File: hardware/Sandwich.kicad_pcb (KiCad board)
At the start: 2 copper layers, 80 x 100.2 mm, 20 parts, among them P1 CONN_01X20, P2 CONN_01X06, P3 VGA_OUT, Q1 PZT2222A, U1 P8X32A-D40, U2 24C512, Y1 5MHz

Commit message: Updated schematics, PCB layout is nearly done.
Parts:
- D1: footprint LEDs:LED-3MM -> LEDs:LED-5MM
- moved Q1 118.8 mm to (187.0, 109.8)
- moved U2 118.5 mm to (209.2, 111.9)
- moved P2 118.1 mm to (180.3, 91.2)
- moved U1 117.7 mm to (178.8, 96.0)
- moved Y1 116.3 mm to (200.0, 108.2)
- moved P1 100.6 mm to (152.0, 144.2)
- moved R7 100.4 mm to (211.4, 144.2)
- moved R11 100.3 mm to (211.4, 140.9)
- moved R6 100.3 mm to (211.4, 137.6)
- moved R10 100.3 mm to (211.4, 134.2)
- moved R5 100.2 mm to (211.4, 130.9)
- moved R9 100.2 mm to (211.4, 127.5)
- moved R4 100.2 mm to (211.4, 124.2)
- moved R8 100.2 mm to (211.4, 120.8)
- moved R1 100.1 mm to (211.4, 117.5)
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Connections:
- P2 pad 5: PROP_DTR -> GND
- P2 pad 6: GND -> PROP_DTR
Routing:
- net 5V: track 0.00 -> 142.7 mm
- net 3.3V: track 45.8 -> 110.0 mm
- net Net-(P1-Pad20): track 0.00 -> 58.1 mm
- net Net-(U1-Pad37): track 0.00 -> 36.0 mm
- net Net-(P1-Pad9): track 0.00 -> 31.0 mm
- net Net-(P1-Pad16): track 0.00 -> 31.0 mm
- net Net-(P1-Pad14): track 0.00 -> 31.0 mm
- net Net-(P1-Pad15): track 0.00 -> 31.0 mm
- net Net-(P1-Pad13): track 0.00 -> 31.0 mm
- net Net-(P1-Pad12): track 0.00 -> 31.0 mm
- net Net-(P1-Pad11): track 0.00 -> 31.0 mm
- net Net-(P1-Pad10): track 0.00 -> 31.0 mm
- net PROP_RX: track 28.2 -> 0.00 mm
- net Net-(R3-Pad1): track 0.00 -> 27.4 mm
- net Net-(C1-Pad1): track 41.8 -> 22.0 mm
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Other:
- board size 80 x 100.2 mm -> 80 x 65 mm

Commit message: Production ready VGA board.
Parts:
- moved C1 49.9 mm to (170.5, 147.8), turned to 180 degrees
- moved R1 33.1 mm to (199.2, 148.2)
- moved P2 30.7 mm to (211.0, 89.5), turned to 270 degrees
- moved Q1 19.3 mm to (186.2, 129.0), turned to 0 degrees
- moved P1 8.50 mm to (160.5, 144.2)
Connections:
- P1 pad 19: PROP_RX -> Net-(P1-Pad19)
- P2 pad 3: PROP_RX -> PROP_TX
- U1 pad 33: Net-(P1-Pad20) -> Net-(P1-Pad17)
- U1 pad 34: PROP_RX -> Net-(P1-Pad18)
- U1 pad 35: Net-(P1-Pad18) -> Net-(P1-Pad19)
- U1 pad 36: Net-(P1-Pad17) -> Net-(P1-Pad20)
- U1 pad 39: PROP_RX -> PROP_TX
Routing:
- net GND: track 107.2 -> 272.1 mm
- net PROP_DTR: track 11.0 -> 111.6 mm
- net 5V: track 142.7 -> 63.1 mm
- net Net-(P1-Pad17): track 0.00 -> 50.5 mm
- net Net-(P1-Pad18): track 0.00 -> 49.5 mm
- net Net-(P1-Pad19): track 0.00 -> 48.9 mm
- net 3.3V: track 110.0 -> 73.1 mm
- net Net-(C1-Pad1): track 22.0 -> 41.5 mm
- net PROP_TX: track 0.00 -> 16.4 mm
- net PROP_RX: track 0.00 -> 12.1 mm
- net Net-(P1-Pad20): track 58.1 -> 48.4 mm
- net Net-(P1-Pad9): track 31.0 -> 22.5 mm
- net Net-(P1-Pad8): track 26.8 -> 18.2 mm
- net Net-(P1-Pad7): track 26.8 -> 18.2 mm
- net Net-(P1-Pad6): track 26.8 -> 18.2 mm
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- added copper zone on B.Cu, net GND

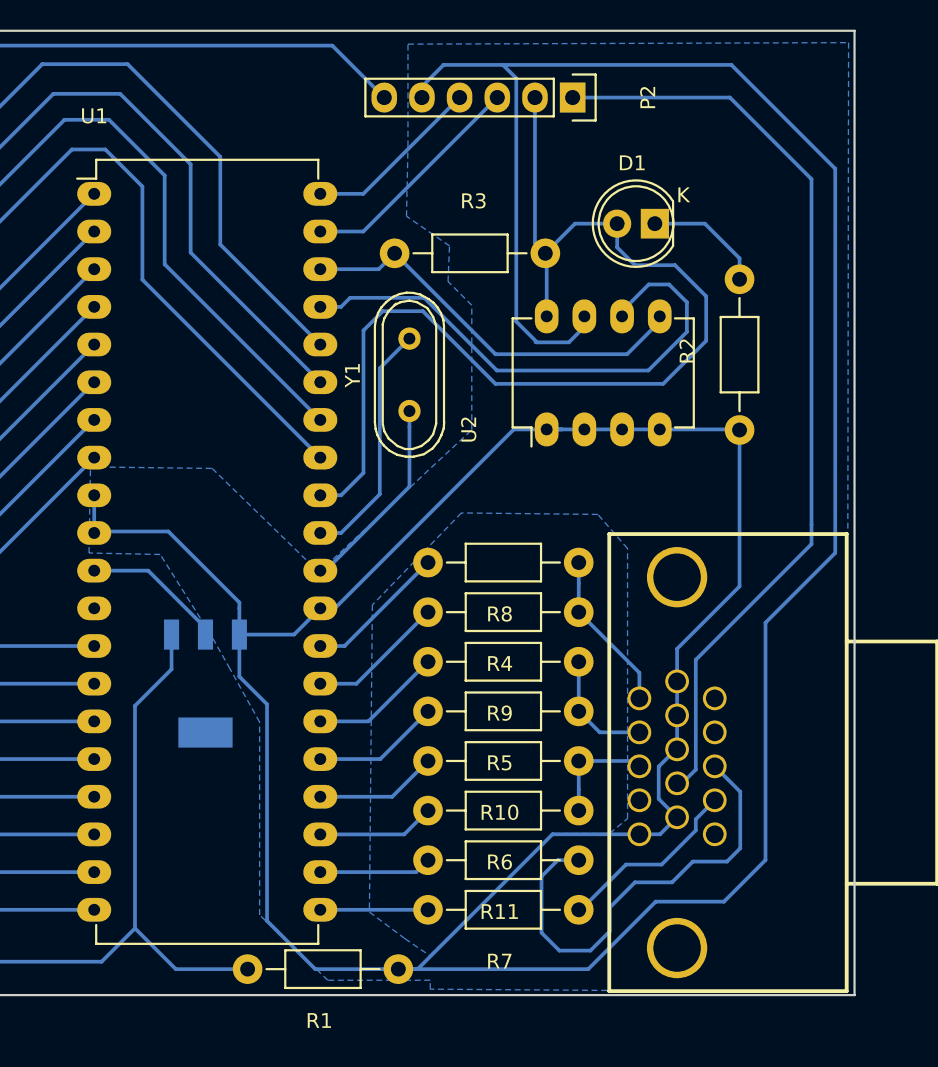
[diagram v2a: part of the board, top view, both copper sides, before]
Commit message: Removed fill area.
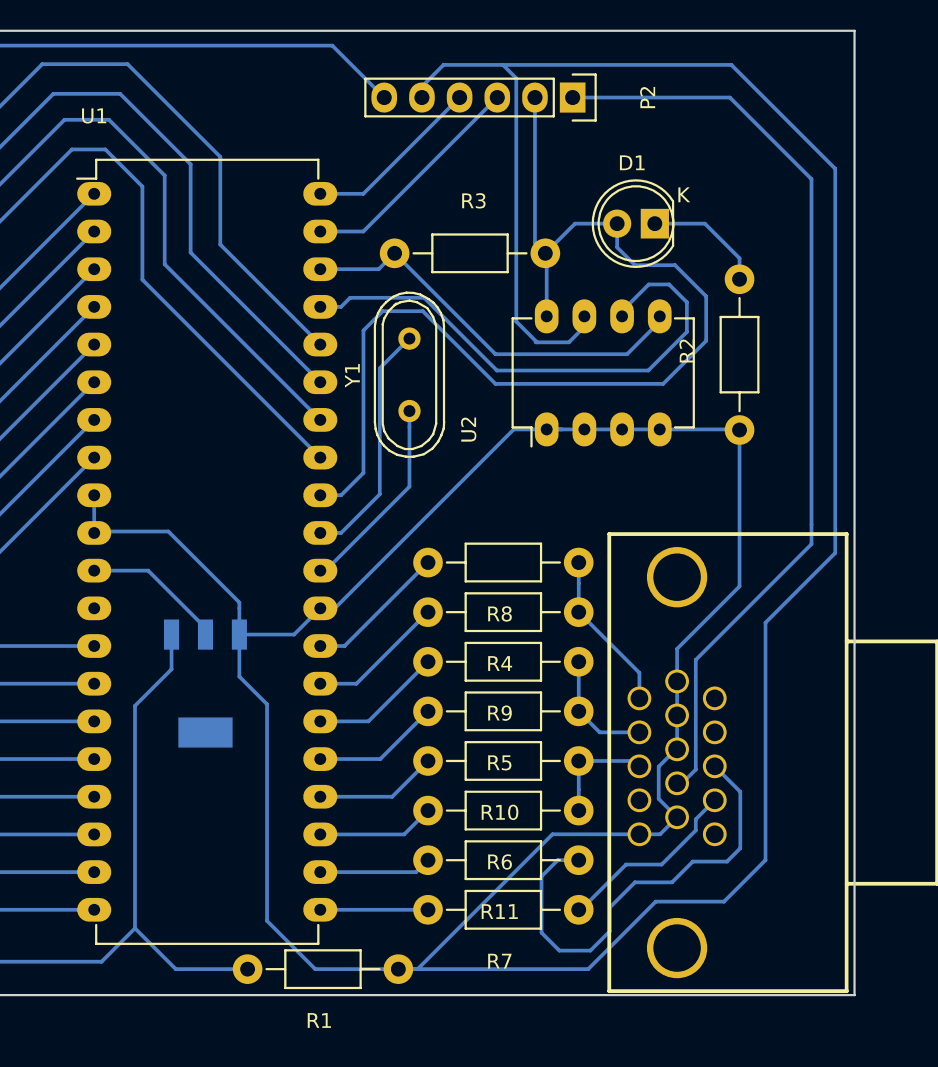
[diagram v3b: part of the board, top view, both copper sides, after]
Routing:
- removed copper zone on B.Cu, net GND
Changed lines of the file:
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@@
     (links 70)
     (no_connects 1)
-    (area 149.924999 84.924999 230.075001 150.075001)
+    (area 149.924999 84.391666 235.893001 166.325002)
     (thickness 1.6)
     (drawings 4)
@@
   (segment (start 196.89 98.53) (end 205.92 89.5) (width 0.25) (layer B.Cu) (net 50))
   (segment (start 193.99 98.53) (end 193.28 98.53) (width 0.25) (layer B.Cu) (net 50))
-  (zone (net 26) (net_name GND) (layer B.Cu) (hatch edge 0.508)
-    (connect_pads (clearance 0.508))
-    (min_thickness 0.254)
-    (fill yes (arc_segments 16) (thermal_gap 0.508) (thermal_bridge_width 0.508))
-    (polygon
-      (pts
-        (xy 229.5 149.8) (xy 201.4 149.6) (xy 201.4 149) (xy 194.5 149) (xy 189.9 144.6)
-        (xy 189.9 131.6) (xy 187.9 128) (xy 186.6 125.7) (xy 183.2 120.3) (xy 178.4 120.2)
-        (xy 178.5 114.4) (xy 186.7 114.5) (xy 193.9 121.5) (xy 204.2 111.9) (xy 204.2 103.5)
-        (xy 202.6 101.9) (xy 202.7 99.5) (xy 199.8 97.5) (xy 199.9 92.8) (xy 199.9 85.9)
-        (xy 229.6 85.8) (xy 229.5 149.8)
-      )
-    )
-    (polygon
-      (pts        (xy 197.5 123.7) (xy 197.3 144.4) (xy 199.7 146.2) (xy 201.4 147.360976) (xy 201.4 147.3)
-        (xy 209.7 139.1) (xy 213.5 139.1) (xy 214.7 138.1) (xy 214.7 119.9) (xy 212.7 117.6)
-        (xy 203.5 117.5) (xy 197.5 123.7)
-      )
-    )
-  )
 )

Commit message: Regenerated both PCBs
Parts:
- moved P3 151.8 mm to (83.0, 64.8)
- moved C1 151.8 mm to (35.5, 78.2)
- moved D1 151.8 mm to (81.5, 28.5)
- moved P1 151.8 mm to (25.5, 74.8)
- moved P2 151.8 mm to (76.0, 20.0)
- moved Q1 151.8 mm to (51.2, 59.5)
- moved R1 151.8 mm to (64.2, 78.8)
- moved R10 151.8 mm to (76.4, 64.7)
- moved R11 151.8 mm to (76.4, 71.4)
- moved R2 151.8 mm to (87.2, 42.4)
- moved R3 151.8 mm to (64.0, 30.5)
- moved R4 151.8 mm to (76.4, 54.7)
- moved R5 151.8 mm to (76.4, 61.4)
- moved R6 151.8 mm to (76.4, 68.1)
- moved R7 151.8 mm to (76.4, 74.8)
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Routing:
- net (no net): track 16.0 -> 0.00 mm

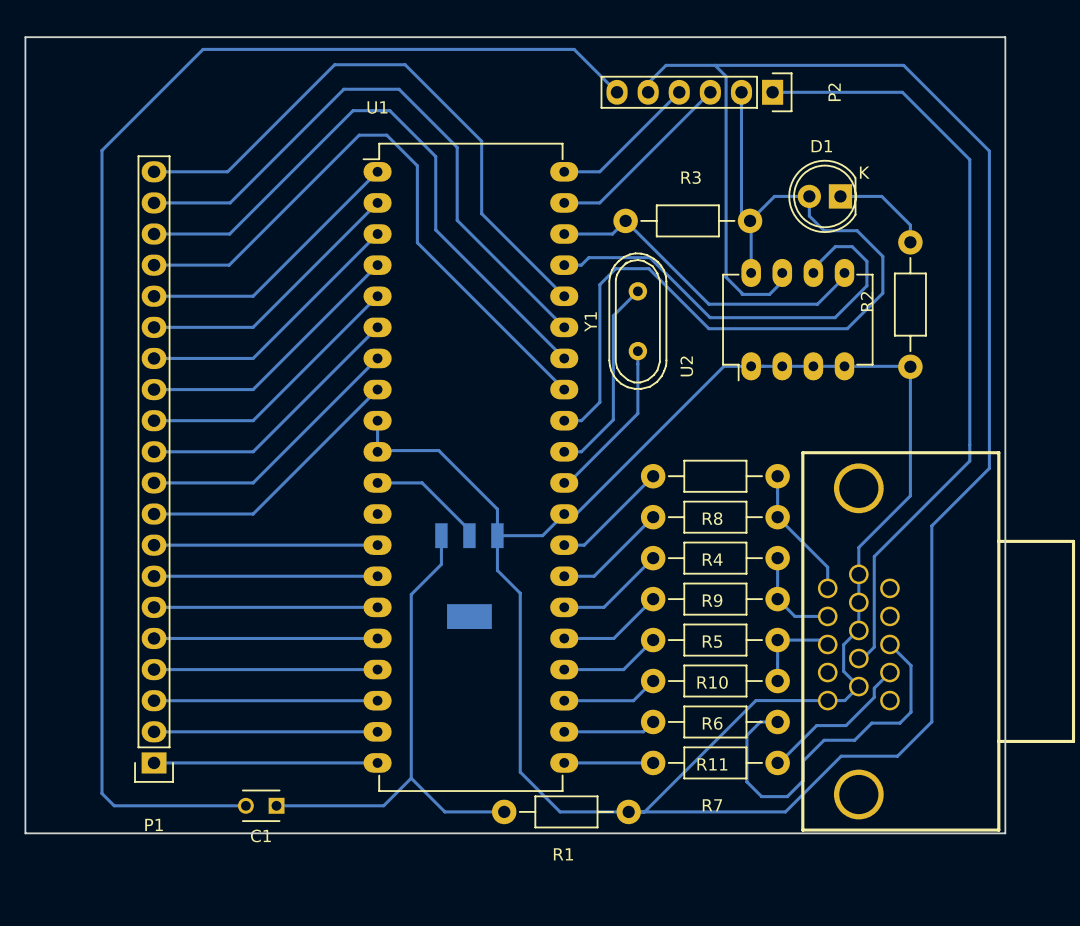
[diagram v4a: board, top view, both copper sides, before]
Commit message: Mounting holes and drill files.
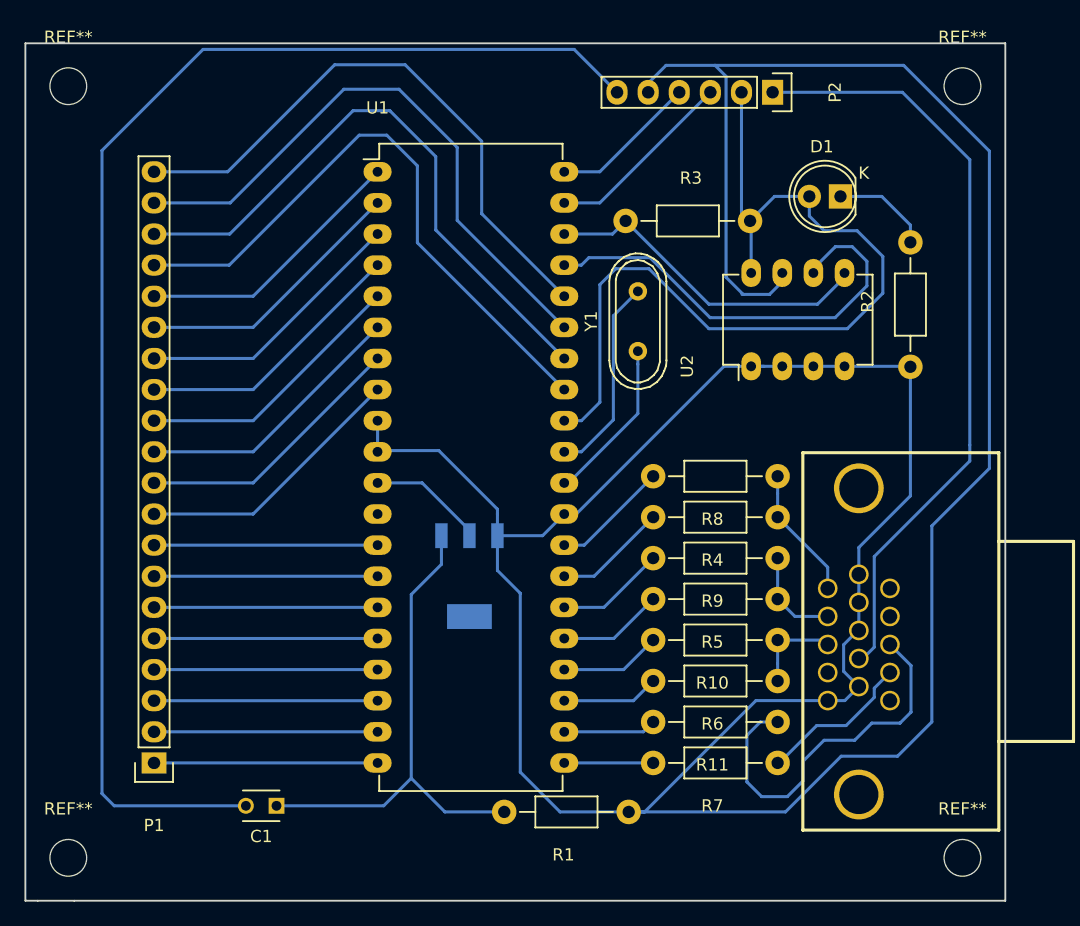
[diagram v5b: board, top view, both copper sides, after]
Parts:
- added REF**: MountingHole_3mm, Mounting_Holes:MountingHole_3mm, F.Cu at (18.5, 19.5)
- added REF**: MountingHole_3mm, Mounting_Holes:MountingHole_3mm, F.Cu at (91.5, 19.5)
- added REF**: MountingHole_3mm, Mounting_Holes:MountingHole_3mm, F.Cu at (18.5, 82.5)
- added REF**: MountingHole_3mm, Mounting_Holes:MountingHole_3mm, F.Cu at (91.5, 82.5)
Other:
- board size 80 x 65 mm -> 80 x 70 mm
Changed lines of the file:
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@@
-(kicad_pcb (version 4) (host pcbnew "(2016-02-14 BZR 6556)-product")
+(kicad_pcb (version 4) (host pcbnew 4.0.2-4+6225~38~ubuntu14.04.1-stable)
   (general
     (links 70)
     (no_connects 1)
-    (area 149.924999 84.391666 235.893001 166.325002)
+    (area 12.011474 14.3745 100.893001 88.47626)
     (thickness 1.6)
-    (drawings 4)
+    (drawings 6)
     (tracks 230)
     (zones 0)
-    (modules 20)
+    (modules 24)
     (nets 51)
   )
@@
     (pad_drill 0.762)
     (pad_to_mask_clearance 0.2)
-    (aux_axis_origin 0 0)
-    (visible_elements FFFFFF7F)
+    (aux_axis_origin 15 86)
+    (visible_elements 7FFFFFFF)
     (pcbplotparams
-      (layerselection 0x00000_fffffffe)
+      (layerselection 0x00000_80000000)
       (usegerberextensions false)
       (excludeedgelayer true)
@@
       (hpglpenspeed 20)
       (hpglpendiameter 15)
+      (hpglpenoverlay 2)
       (psnegative false)
       (psa4output false)
@@
     )
   )
-  (gr_line (start 15 15.5) (end 15 80.5) (layer Edge.Cuts) (width 0.15))
-  (gr_line (start 95 15.5) (end 15 15.5) (layer Edge.Cuts) (width 0.15))
-  (gr_line (start 95 80.5) (end 95 15.5) (layer Edge.Cuts) (width 0.15))
-  (gr_line (start 15 80.5) (end 95 80.5) (layer Edge.Cuts) (width 0.15))
+  (module Mounting_Holes:MountingHole_3mm (layer F.Cu)
+    (at 18.5 19.5)
+    (descr "Mounting hole, Befestigungsbohrung, 3mm, No Annular, Kein Restring,")
+    (tags "Mounting hole, Befestigungsbohrung, 3mm, No Annular, Kein Restring,")
+    (fp_text reference REF** (at 0 -4.0005) (layer F.SilkS)
+      (effects (font (size 1 1) (thickness 0.15)))
+    )
+    (fp_text value MountingHole_3mm (at 1.00076 5.00126) (layer F.Fab)
+      (effects (font (size 1 1) (thickness 0.15)))
+    )
+    (fp_circle (center 0 0) (end 3 0) (layer Cmts.User) (width 0.381))
+    (pad 1 thru_hole circle (at 0 0) (size 3 3) (drill 3) (layers))
+  )
+  (module Mounting_Holes:MountingHole_3mm (layer F.Cu)
+    (at 91.5 19.5)
+    (descr "Mounting hole, Befestigungsbohrung, 3mm, No Annular, Kein Restring,")
+    (tags "Mounting hole, Befestigungsbohrung, 3mm, No Annular, Kein Restring,")
+    (fp_text reference REF** (at 0 -4.0005) (layer F.SilkS)
+      (effects (font (size 1 1) (thickness 0.15)))
+    )
+    (fp_text value MountingHole_3mm (at 1.00076 5.00126) (layer F.Fab)
+      (effects (font (size 1 1) (thickness 0.15)))
+    )
+    (fp_circle (center 0 0) (end 3 0) (layer Cmts.User) (width 0.381))
+    (pad 1 thru_hole circle (at 0 0) (size 3 3) (drill 3) (layers))
+  )
+  (module Mounting_Holes:MountingHole_3mm (layer F.Cu)
+    (at 18.5 82.5)
+    (descr "Mounting hole, Befestigungsbohrung, 3mm, No Annular, Kein Restring,")
+    (tags "Mounting hole, Befestigungsbohrung, 3mm, No Annular, Kein Restring,")
+    (fp_text reference REF** (at 0 -4.0005) (layer F.SilkS)
+      (effects (font (size 1 1) (thickness 0.15)))
+    )
+    (fp_text value MountingHole_3mm (at 1.00076 5.00126) (layer F.Fab)
+      (effects (font (size 1 1) (thickness 0.15)))
+    )
+    (fp_circle (center 0 0) (end 3 0) (layer Cmts.User) (width 0.381))
+    (pad 1 thru_hole circle (at 0 0) (size 3 3) (drill 3) (layers))
+  )
+  (module Mounting_Holes:MountingHole_3mm (layer F.Cu)
+    (at 91.5 82.5)
+    (descr "Mounting hole, Befestigungsbohrung, 3mm, No Annular, Kein Restring,")
+    (tags "Mounting hole, Befestigungsbohrung, 3mm, No Annular, Kein Restring,")
+    (fp_text reference REF** (at 0 -4.0005) (layer F.SilkS)
+      (effects (font (size 1 1) (thickness 0.15)))
+    )
+    (fp_text value MountingHole_3mm (at 1.00076 5.00126) (layer F.Fab)
+      (effects (font (size 1 1) (thickness 0.15)))
+    )
+    (fp_circle (center 0 0) (end 3 0) (layer Cmts.User) (width 0.381))
+    (pad 1 thru_hole circle (at 0 0) (size 3 3) (drill 3) (layers))
+  )
+  (gr_line (start 15 86) (end 16 86) (angle 90) (layer Edge.Cuts) (width 0.15))
+  (gr_line (start 15 16) (end 15 86) (angle 90) (layer Edge.Cuts) (width 0.15))
+  (gr_line (start 19 86) (end 16 86) (angle 90) (layer Edge.Cuts) (width 0.15))
+  (gr_line (start 95 86) (end 19 86) (angle 90) (layer Edge.Cuts) (width 0.15))
+  (gr_line (start 95 16) (end 95 86) (angle 90) (layer Edge.Cuts) (width 0.15))
+  (gr_line (start 15 16) (end 95 16) (angle 90) (layer Edge.Cuts) (width 0.15))
   (segment (start 35.5 78.25) (end 44.25 78.25) (width 0.25) (layer B.Cu) (net 1))
   (segment (start 44.25 78.25) (end 46.5 76) (width 0.25) (layer B.Cu) (net 1))
